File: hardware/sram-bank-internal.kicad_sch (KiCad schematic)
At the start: 10 parts, among them U1 74LVC138A

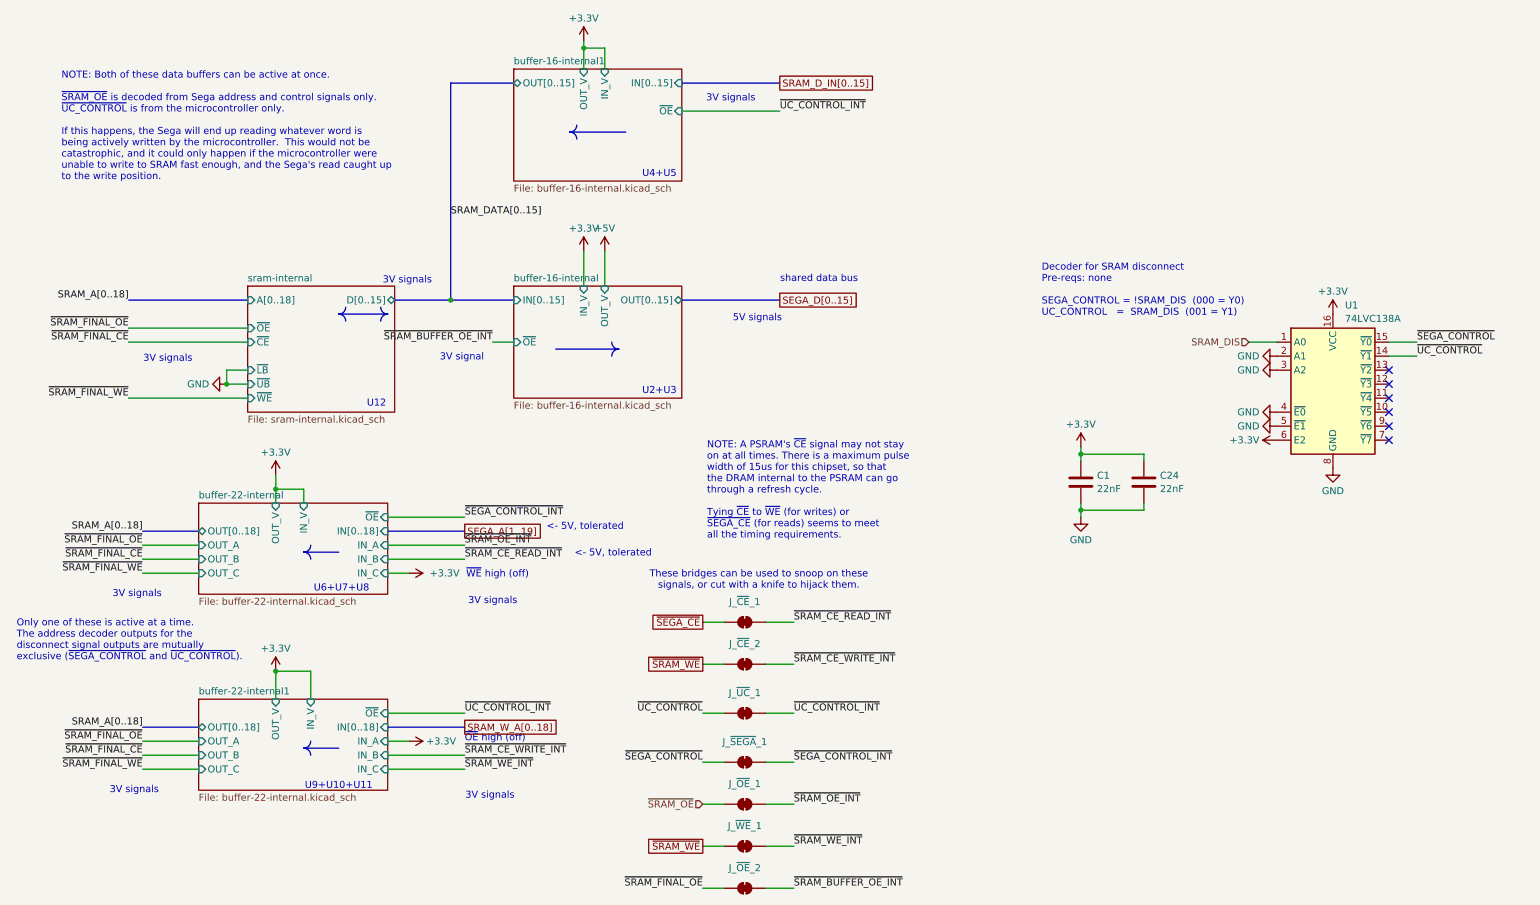
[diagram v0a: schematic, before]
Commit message: Reannotate schematics and drop debug bridges
Parts are now numbered starting at 0 for cart, 100 for SRAM, 300 for
microcontroller.

Also, drop debug bridges that made routing more difficult and had the
same names across prototype boards.

Hopefully this will help avoid naming conflicts for the unified PCB.

Also, redo prototype PCB layouts.

Now that all the names have changed, update board layouts.
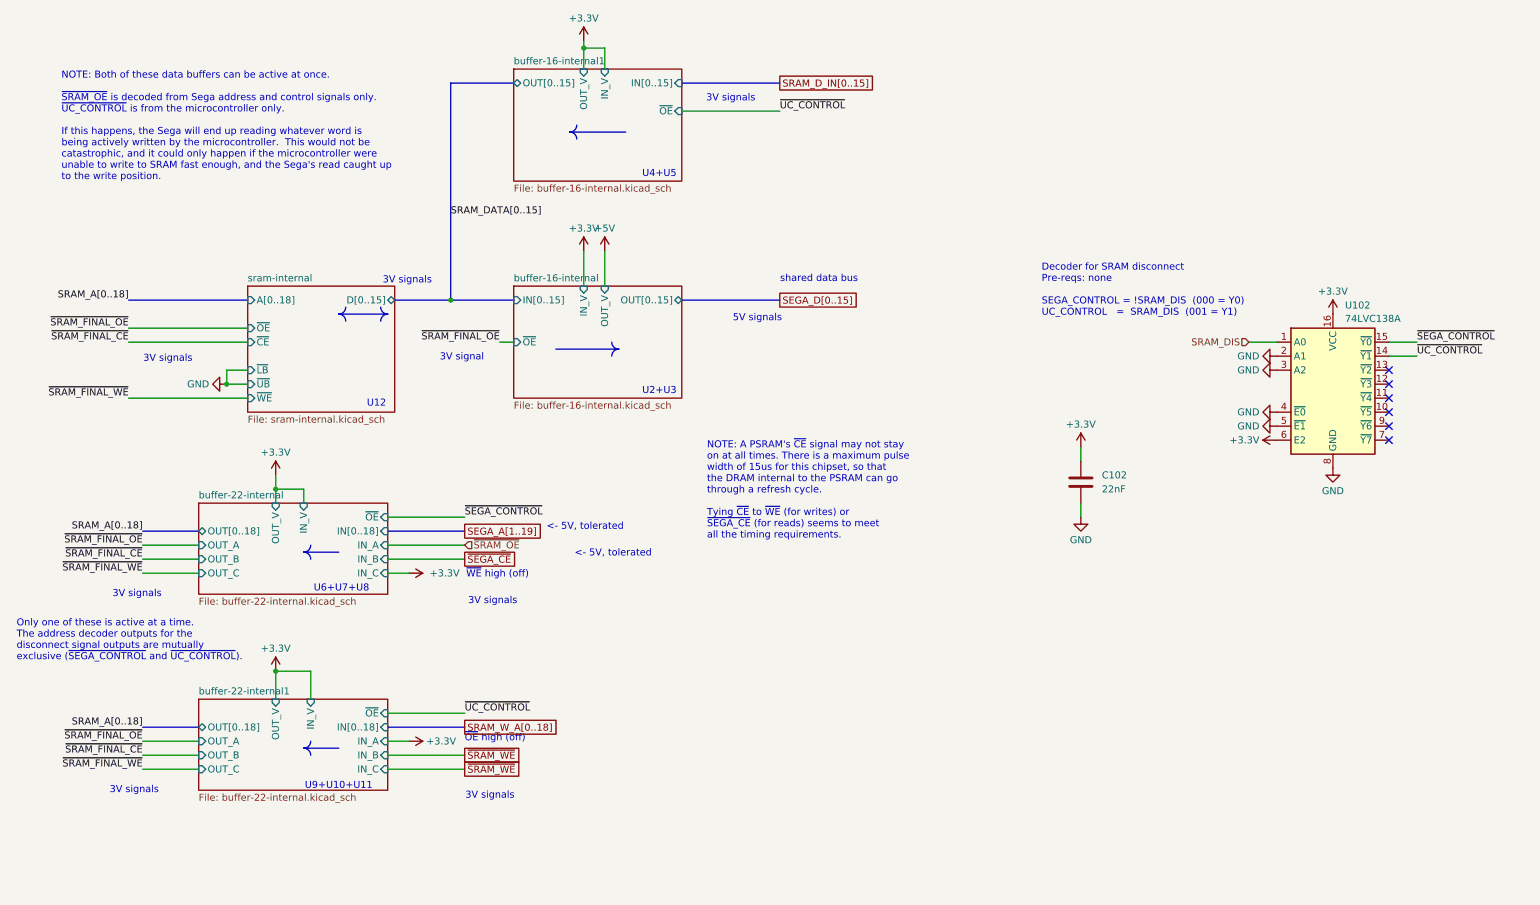
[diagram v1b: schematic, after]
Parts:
- removed C24: 22nF, Capacitor_SMD:C_0603_1608Metric, symbol Device:C
- removed J_~{CE}_1, J_~{CE}_2, J_~{OE}_1, J_~{OE}_2, J_~{SEGA}_1, J_~{UC}_1, J_~{WE}_1: ~, Jumper:SolderJumper-2_P1.3mm_Bridged_RoundedPad1.0x1.5mm, symbol Jumper:SolderJumper_2_Bridged
- renumbered C1 to C102, U1 to U102
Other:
- note removed: "These bridges can be used to snoop on these signals, or cut with a knife to hijack them."
